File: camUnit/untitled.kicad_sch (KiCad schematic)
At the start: 2 parts, among them SW1 SW_SPDT, U1 Teensy 4.0

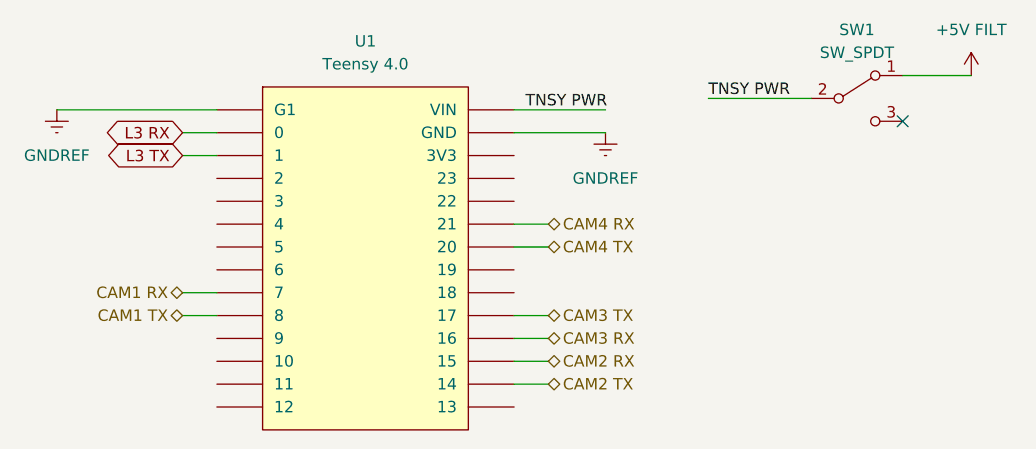
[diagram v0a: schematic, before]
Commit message: m1n footprint
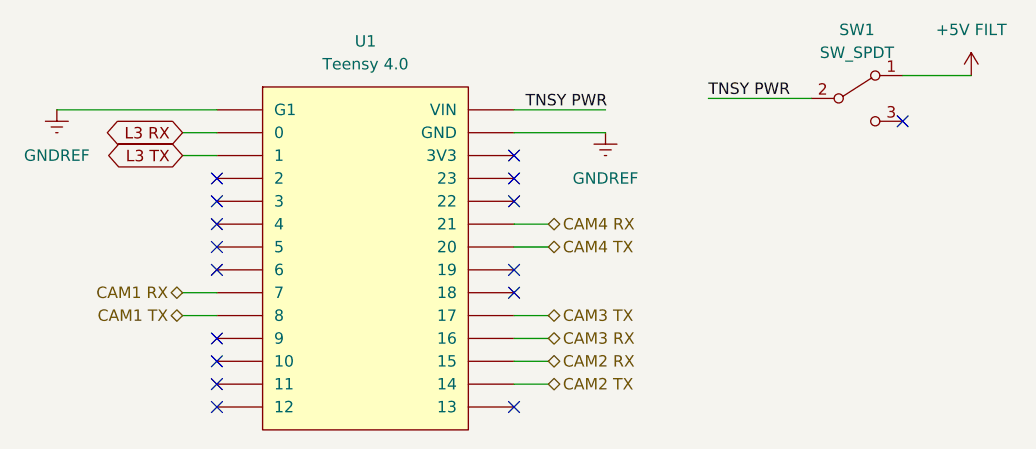
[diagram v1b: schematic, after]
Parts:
- U1: footprint (none) -> Library:Teensy 4.0
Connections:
- no-connect marks 1 -> 16
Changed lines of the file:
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@@
 	(paper "A4")
 	(no_connect
+		(at 44.45 62.23)
+	)
+	(no_connect
+		(at 44.45 44.45)
+	)
+	(no_connect
+		(at 44.45 54.61)
+	)
+	(no_connect
+		(at 44.45 49.53)
+	)
+	(no_connect
+		(at 77.47 44.45)
+	)
+	(no_connect
+		(at 44.45 67.31)
+	)
+	(no_connect
+		(at 44.45 69.85)
+	)
+	(no_connect
 		(at 120.65 38.1)
+	)
+	(no_connect
+		(at 77.47 69.85)
+	)
+	(no_connect
+		(at 77.47 46.99)
+	)
+	(no_connect
+		(at 77.47 41.91)
+	)
+	(no_connect
+		(at 77.47 57.15)
+	)
+	(no_connect
+		(at 44.45 46.99)
+	)
+	(no_connect
+		(at 77.47 54.61)
+	)
+	(no_connect
+		(at 44.45 64.77)
+	)
+	(no_connect
+		(at 44.45 52.07)
 	)
 	(wire
@@
 			)
 		)
-		(property "Footprint" ""
+		(property "Footprint" "Library:Teensy 4.0"
 			(at 60.96 57.15 0)
 			(effects
